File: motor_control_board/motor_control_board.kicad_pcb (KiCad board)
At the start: 4 copper layers, 45 x 40 mm, 78 parts, among them J1 Conn_01x05_Female, J2 Conn_01x05_Female, J3 Harwin_G125-MG10605M4P, J4 Harwin_M80-5000000M5-02-333-0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, J5 Harwin_M80-5400642, J6 Harwin_M80-8510442, J7 Harwin_M80-8510442, U1 CPC1117N, U2 MCP2562, U3 PIC18F26K83, U4 MCP2562, U5 PIC18F26K83, U6 SN74LVC1G14DBV, U7 INA232AIDDFR, U8 UA78M05IDCYR, U9 ECH8420-TL-H, X1 12MHz, X2 12MHz

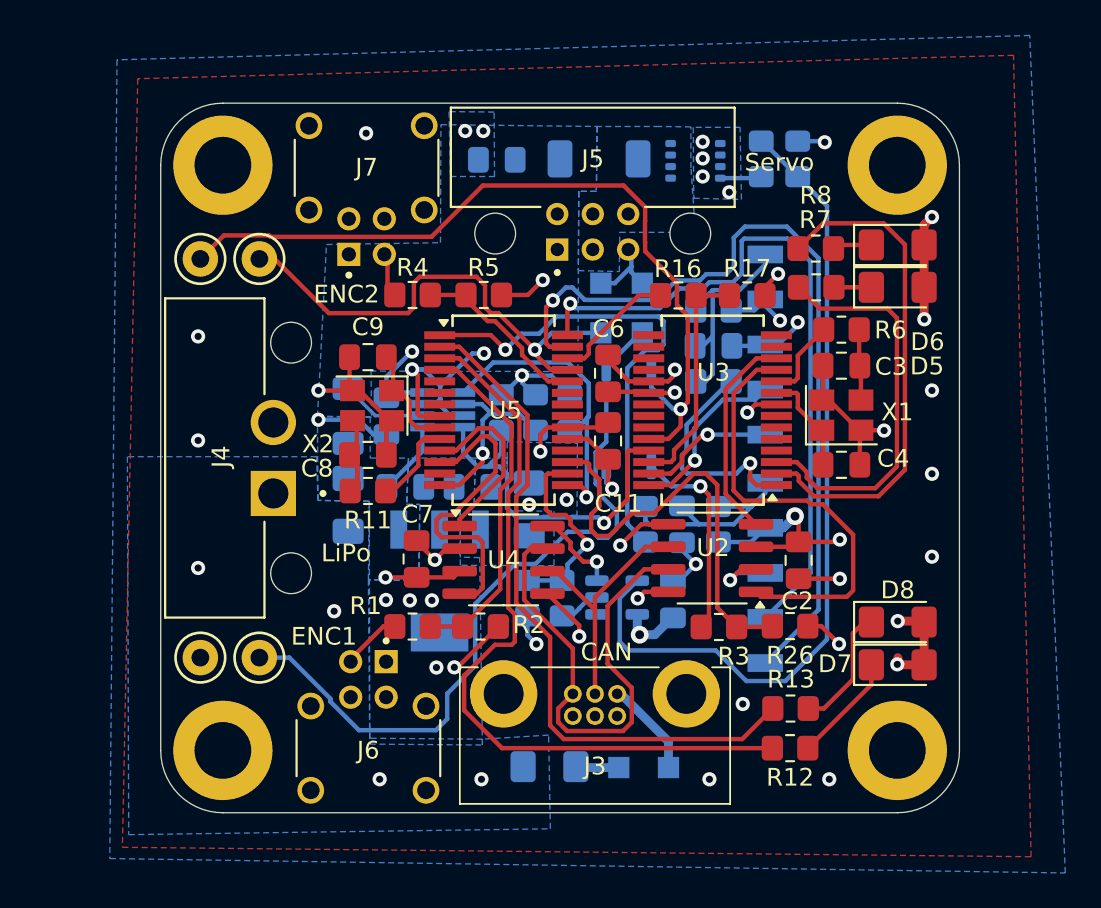
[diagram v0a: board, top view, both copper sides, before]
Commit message: Added servo power LED, bulk decoupling caps
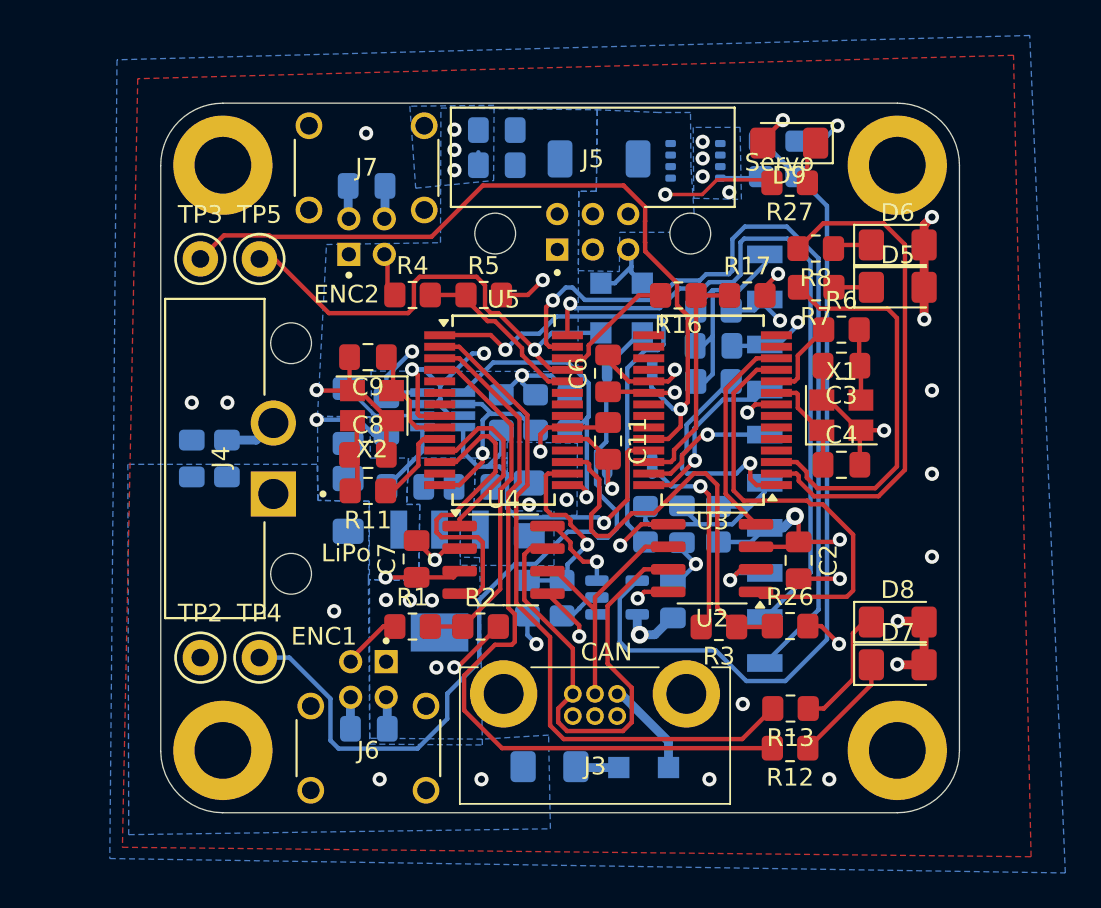
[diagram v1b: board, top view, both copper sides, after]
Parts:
- added C16: 100n, Capacitor_SMD:C_0805_2012Metric_Pad1.18x1.45mm_HandSolder, B.Cu at (162.2, 92.3)
- added C17: 100n, Capacitor_SMD:C_0805_2012Metric_Pad1.18x1.45mm_HandSolder, B.Cu at (162.1, 61.7)
- added C18: 22u, Capacitor_SMD:C_0805_2012Metric_Pad1.18x1.45mm_HandSolder, B.Cu at (152.2, 77.0)
- added C19: 22u, Capacitor_SMD:C_0805_2012Metric_Pad1.18x1.45mm_HandSolder, B.Cu at (154.2, 77.0)
- added C21: 22u, Capacitor_SMD:C_0805_2012Metric_Pad1.18x1.45mm_HandSolder, B.Cu at (169.4, 58.5)
- added D9: RED, LED_SMD:LED_1206_3216Metric_Pad1.42x1.75mm_HandSolder, F.Cu at (185.9, 59.3)
- added R27: 330R, Resistor_SMD:R_0805_2012Metric_Pad1.20x1.40mm_HandSolder, F.Cu at (185.9, 61.5)
- C1: value 10u -> 22u; footprint canhw_footprints:C_0805_2012Metric_Pad1.18x1.45mm_HandSolder -> Capacitor_SMD:C_0805_2012Metric_Pad1.18x1.45mm_HandSolder
- C10, C11, C12, C13, C14, C15, C2, C3, C4, C5, C6, C7, C8, C9: footprint canhw_footprints:C_0805_2012Metric_Pad1.18x1.45mm_HandSolder -> Capacitor_SMD:C_0805_2012Metric_Pad1.18x1.45mm_HandSolder
- D1, D2, D3: footprint canhw_footprints:Nexperia_CFP3_SOD-123W -> Diode_SMD:Nexperia_CFP3_SOD-123W
- D4: footprint canhw_footprints:D_SOD-128 -> Diode_SMD:D_SOD-128
- D5, D6, D7, D8: footprint canhw_footprints:LED_1206_3216Metric_Pad1.42x1.75mm_HandSolder -> LED_SMD:LED_1206_3216Metric_Pad1.42x1.75mm_HandSolder
- F1, F2, F3: footprint canhw_footprints:Fuse_1206_3216Metric_Pad1.42x1.75mm_HandSolder -> Fuse:Fuse_1206_3216Metric_Pad1.42x1.75mm_HandSolder
- H1, H2, H3, H4: footprint canhw_footprints:MountingHole_3.2mm_M3_DIN965_Pad -> MountingHole:MountingHole_3.2mm_M3_DIN965_Pad
- R1, R10, R11, R12, R13, R14, R15, R16, R17, R18, R19, R2, R20, R21, R23, R24, R25, R26, R3, R4, R5, R6, R7, R8, R9: footprint canhw_footprints:R_0805_2012Metric_Pad1.20x1.40mm_HandSolder -> Resistor_SMD:R_0805_2012Metric_Pad1.20x1.40mm_HandSolder
- R22: footprint canhw_footprints:R_1206_3216Metric_Pad1.30x1.75mm_HandSolder -> Resistor_SMD:R_1206_3216Metric_Pad1.30x1.75mm_HandSolder
- TP2, TP3, TP4, TP5: footprint canhw_footprints:TestPoint_Keystone_5000-5004_Miniature -> TestPoint:TestPoint_Keystone_5000-5004_Miniature
- U1: footprint canhw_footprints:SOP-4_3.8x4.1mm_P2.54mm -> canhw_footprints:SOIC254P610X218-4N
- U2, U4: footprint canhw_footprints:SOIC-8_3.9x4.9mm_P1.27mm -> Package_SO:SOIC-8_3.9x4.9mm_P1.27mm
- U3, U5: footprint canhw_footprints:SSOP-28_5.3x10.2mm_P0.65mm -> Package_SO:SSOP-28_5.3x10.2mm_P0.65mm
- U6: footprint canhw_footprints:SOT-23-5 -> Package_TO_SOT_SMD:SOT-23-5
- U9: footprint canhw_footprints:OnSemi_ECH8 -> Package_TO_SOT_SMD:OnSemi_ECH8
- X1, X2: footprint canhw_footprints:Crystal_SMD_Abracon_ABM8G-4Pin_3.2x2.5mm -> Crystal:Crystal_SMD_Abracon_ABM8G-4Pin_3.2x2.5mm
- moved C1 0.30 mm to (169.4, 60.5)
- moved U1 0.05 mm to (176.9, 74.7)
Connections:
- J6 pad 1: +5V -> unconnected-(J6-Pin_1-Pad1)
- J6 pad 3: GND -> +5V
- J6 pad 4: unconnected-(J6-Pin_4-Pad4) -> GND
- J7 pad 1: +5V -> unconnected-(J7-Pin_1-Pad1)
- J7 pad 3: GND -> +5V
- J7 pad 4: unconnected-(J7-Pin_4-Pad4) -> GND
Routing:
- net GND: track 84.4 -> 92.3 mm
- net /Servo-: track 0.00 -> 6.42 mm, vias 0 -> 1
- net +5V: track 62.3 -> 67.7 mm, vias 17 -> 18
- net Net-(D9-K): track 0.00 -> 2.43 mm
- net /PWM_SERVO: track 42.4 -> 44.5 mm

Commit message: silkscreen
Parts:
- added G***: LOGO, Team_Logo:Logo_SilkScreen_5mm, B.Cu at (170.6, 68.1)
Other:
- board text added: "5V"

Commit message: Free some Real estate so Joe can move in
Moved things around, generate production files
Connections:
- net /MCLR_FS renamed /Failsafe MCU/MCLR_FS
- J1 pad 1: /ICSPCLK_FS -> /Failsafe MCU/ICSPDAT_FS
- J1 pad 2: /ICSPDAT_FS -> /Failsafe MCU/ICSPCLK_FS
- U5 pad 27: /ICSPCLK_FS -> /Failsafe MCU/ICSPCLK_FS
- U5 pad 28: /ICSPDAT_FS -> /Failsafe MCU/ICSPDAT_FS
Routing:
- net (no net): track 0.00 -> 87.1 mm, vias 0 -> 2
- net /ICSPCLK_FS: track 47.2 -> 0.00 mm, vias 1 -> 0
- net /ICSPDAT_FS: track 39.9 -> 0.00 mm, vias 1 -> 0

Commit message: skill issued two pinouts
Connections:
- J1 pad 1: /Failsafe MCU/ICSPDAT_FS -> /Failsafe MCU/ICSPCLK_FS
- J1 pad 2: /Failsafe MCU/ICSPCLK_FS -> /Failsafe MCU/ICSPDAT_FS
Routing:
- net (no net): track 87.1 -> 0.00 mm, vias 2 -> 0
- net /Failsafe MCU/ICSPCLK_FS: track 0.00 -> 47.2 mm, vias 0 -> 1
- net /Failsafe MCU/ICSPDAT_FS: track 0.00 -> 39.9 mm, vias 0 -> 1

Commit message: Address concerns
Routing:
- net GND: track 92.7 -> 92.3 mm, vias 44 -> 46
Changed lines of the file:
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@@
 	)
 	(segment
+		(start 170.115863 67.818)
+		(end 171.388278 69.090415)
+		(width 0.25)
+		(layer "F.Cu")
+		(net 2)
+	)
+	(segment
 		(start 187.7861 73.6809)
 		(end 187.7236 73.7434)
@@
 	)
 	(segment
-		(start 169.656 67.818)
-		(end 171.1452 67.818)
-		(width 0.25)
-		(layer "F.Cu")
-		(net 2)
-	)
-	(segment
 		(start 179.0588 84.5566)
 		(end 177.706104 84.5566)
@@
 	)
 	(segment
-		(start 171.1452 67.818)
-		(end 171.9834 66.9798)
-		(width 0.25)
-		(layer "F.Cu")
-		(net 2)
-	)
-	(segment
 		(start 164.8714 81.6649)
 		(end 164.8714 81.723227)
@@
 	)
 	(segment
+		(start 169.656 67.818)
+		(end 170.115863 67.818)
+		(width 0.25)
+		(layer "F.Cu")
+		(net 2)
+	)
+	(segment
 		(start 177.9592 72.689)
 		(end 179.0592 72.689)
@@
 	)
 	(via
-		(at 171.9834 66.9798)
+		(at 171.388278 69.090415)
 		(size 0.8)
 		(drill 0.4)
@@
 	)
 	(via
+		(at 182.5 58)
+		(size 0.8)
+		(drill 0.4)
+		(layers "F.Cu" "B.Cu")
+		(free yes)
+		(net 2)
+	)
+	(via
 		(at 165.989 88.8238)
 		(size 0.8)
@@
 	)
 	(via
+		(at 181.5 58)
+		(size 0.8)
+		(drill 0.4)
+		(layers "F.Cu" "B.Cu")
+		(free yes)
+		(net 2)
+	)
+	(via
 		(at 167.132 60.7822)
 		(size 0.8)
@@
 		(polygon
 			(pts
-				(xy 162.3314 74.7014) (xy 159.2834 74.676) (xy 159.7914 64.9732) (xy 166.2176 64.8716) (xy 166.243 57.277)
-				(xy 175.0568 57.3786) (xy 175.006 61.976) (xy 174.0154 61.976) (xy 173.9646 72.136) (xy 162.306 72.1106)
+				(xy 162.3314 74.7014) (xy 159.2834 74.676) (xy 160 63) (xy 166 62) (xy 166.243 57.277) (xy 175.0568 57.3786)
+				(xy 175.006 61.976) (xy 174.0154 61.976) (xy 173.9646 72.136) (xy 162.306 72.1106)
 			)
 		)

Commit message: addressed concerns
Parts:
- added C20: 22u, canhw_footprints:C_0805_2012Metric_Pad1.18x1.45mm_HandSolder, B.Cu at (148.1, 77.0)
- C1, C10, C11, C12, C13, C14, C15, C16, C17, C18, C19, C2, C21, C3, C4, C5, C6, C7, C8, C9: footprint Capacitor_SMD:C_0805_2012Metric_Pad1.18x1.45mm_HandSolder -> canhw_footprints:C_0805_2012Metric_Pad1.18x1.45mm_HandSolder
- D1, D2, D3: footprint Diode_SMD:Nexperia_CFP3_SOD-123W -> canhw_footprints:Nexperia_CFP3_SOD-123W
- D4: footprint Diode_SMD:D_SOD-128 -> canhw_footprints:D_SOD-128
- D5, D6, D7, D8, D9: footprint LED_SMD:LED_1206_3216Metric_Pad1.42x1.75mm_HandSolder -> canhw_footprints:LED_1206_3216Metric_Pad1.42x1.75mm_HandSolder
- F1, F2: footprint Fuse:Fuse_1206_3216Metric_Pad1.42x1.75mm_HandSolder -> canhw_footprints:Fuse_1206_3216Metric_Pad1.42x1.75mm_HandSolder
- F3: value Polyfuse 1A -> Polyfuse 0.5A; footprint Fuse:Fuse_1206_3216Metric_Pad1.42x1.75mm_HandSolder -> canhw_footprints:Fuse_1206_3216Metric_Pad1.42x1.75mm_HandSolder
- H1, H2, H3, H4: footprint MountingHole:MountingHole_3.2mm_M3_DIN965_Pad -> canhw_footprints:MountingHole_3.2mm_M3_DIN965_Pad
- J4: footprint canhw_footprints:HARWIN_M80-5000000M5-02-333-00-000 -> canhw_footprints:TE_2-1437667-4
- R1, R10, R11, R12, R13, R14, R15, R16, R17, R18, R19, R2, R20, R21, R23, R24, R25, R26, R27, R3, R4, R5, R6, R7, R8, R9: footprint Resistor_SMD:R_0805_2012Metric_Pad1.20x1.40mm_HandSolder -> canhw_footprints:R_0805_2012Metric_Pad1.20x1.40mm_HandSolder
- R22: footprint Resistor_SMD:R_1206_3216Metric_Pad1.30x1.75mm_HandSolder -> canhw_footprints:R_1206_3216Metric_Pad1.30x1.75mm_HandSolder
- TP2, TP3, TP4, TP5: footprint TestPoint:TestPoint_Keystone_5000-5004_Miniature -> canhw_footprints:TestPoint_Keystone_5000-5004_Miniature
- U2, U4: footprint Package_SO:SOIC-8_3.9x4.9mm_P1.27mm -> canhw_footprints:SOIC-8_3.9x4.9mm_P1.27mm
- U3, U5: footprint Package_SO:SSOP-28_5.3x10.2mm_P0.65mm -> canhw_footprints:SSOP-28_5.3x10.2mm_P0.65mm
- U6: footprint Package_TO_SOT_SMD:SOT-23-5 -> canhw_footprints:SOT-23-5
- U9: footprint Package_TO_SOT_SMD:OnSemi_ECH8 -> canhw_footprints:OnSemi_ECH8
- X1, X2: footprint Crystal:Crystal_SMD_Abracon_ABM8G-4Pin_3.2x2.5mm -> canhw_footprints:Crystal_SMD_Abracon_ABM8G-4Pin_3.2x2.5mm
- moved TP3 5.39 mm to (147.3, 65.9)
- moved TP5 5.39 mm to (150.6, 65.9)
- moved TP2 5.39 mm to (147.3, 88.3)
- moved TP4 5.39 mm to (150.6, 88.3)
- moved H2 5.11 mm to (148.8, 60.5)
- moved H3 5.11 mm to (148.8, 93.5)
- moved J4 4.11 mm to (156.0, 73.0)
- moved G*** 2.54 mm to (168.1, 68.5)
- moved C18 1.94 mm to (150.3, 77.0)
- moved C19 1.78 mm to (152.4, 77.0)
- moved D9 0.18 mm to (185.7, 59.3)
- moved J6 0.13 mm to (162.0, 93.3)
- moved R1 0.13 mm to (164.8, 86.5)
- moved H1 0.05 mm to (192.0, 60.5)
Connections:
- net /ENC1_IN renamed Net-(J6-Pin_2)
- net /ENC2_IN renamed Net-(J7-Pin_2)
- net /Power/LDO_OUT renamed Net-(U8-OUTPUT)
- J4 pad 1: /Batt+ -> GND
- J4 pad 2: GND -> /Batt+
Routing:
- net /PWM_FS: track 27.4 -> 32.8 mm
- net /PWM_MCU: track 46.3 -> 51.7 mm
- net /PWM_SERVO: track 44.5 -> 49.8 mm
- net GND: track 92.3 -> 89.0 mm
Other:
- board size 45 x 40 mm -> 50.2 x 40 mm
- board text added: "+"
- board text added: "MCLR"
- board text added: "Motor Control"
- board text removed: "Missile Control"

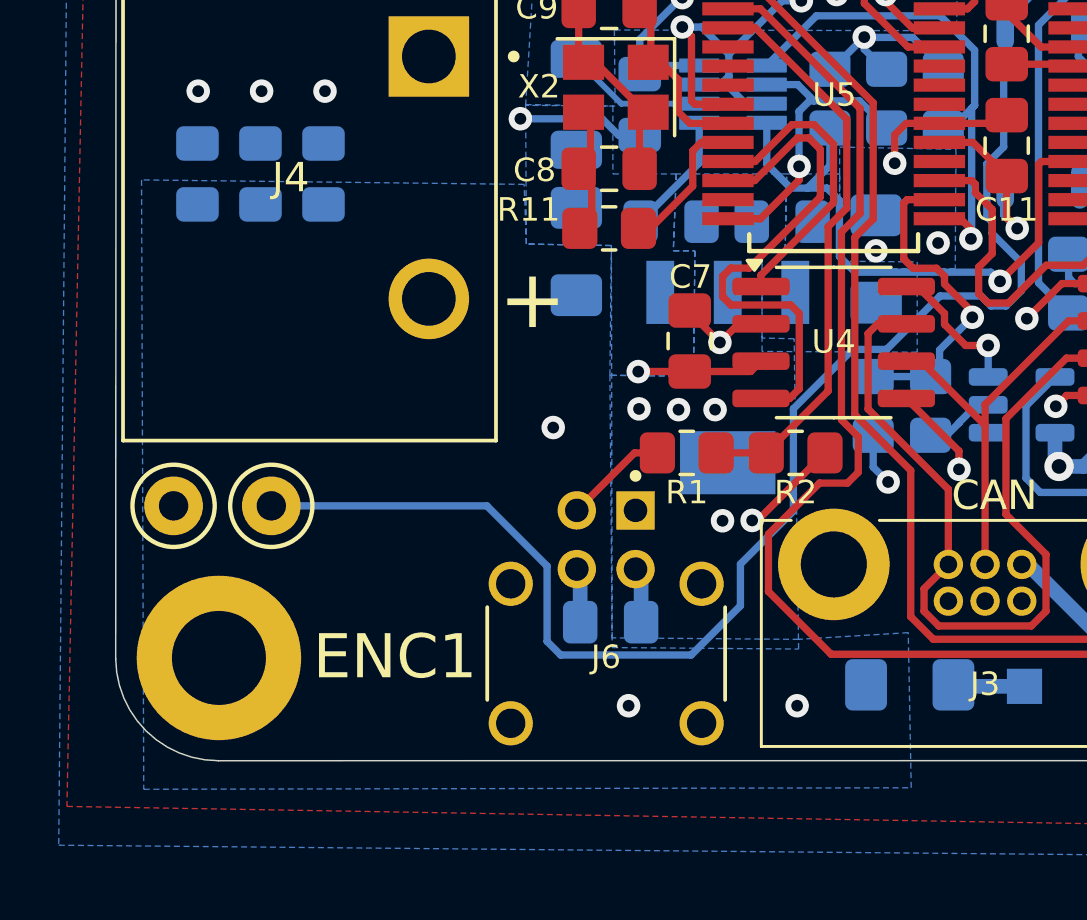
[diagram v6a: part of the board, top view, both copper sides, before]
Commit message: minor schematic and copper pour cleanup
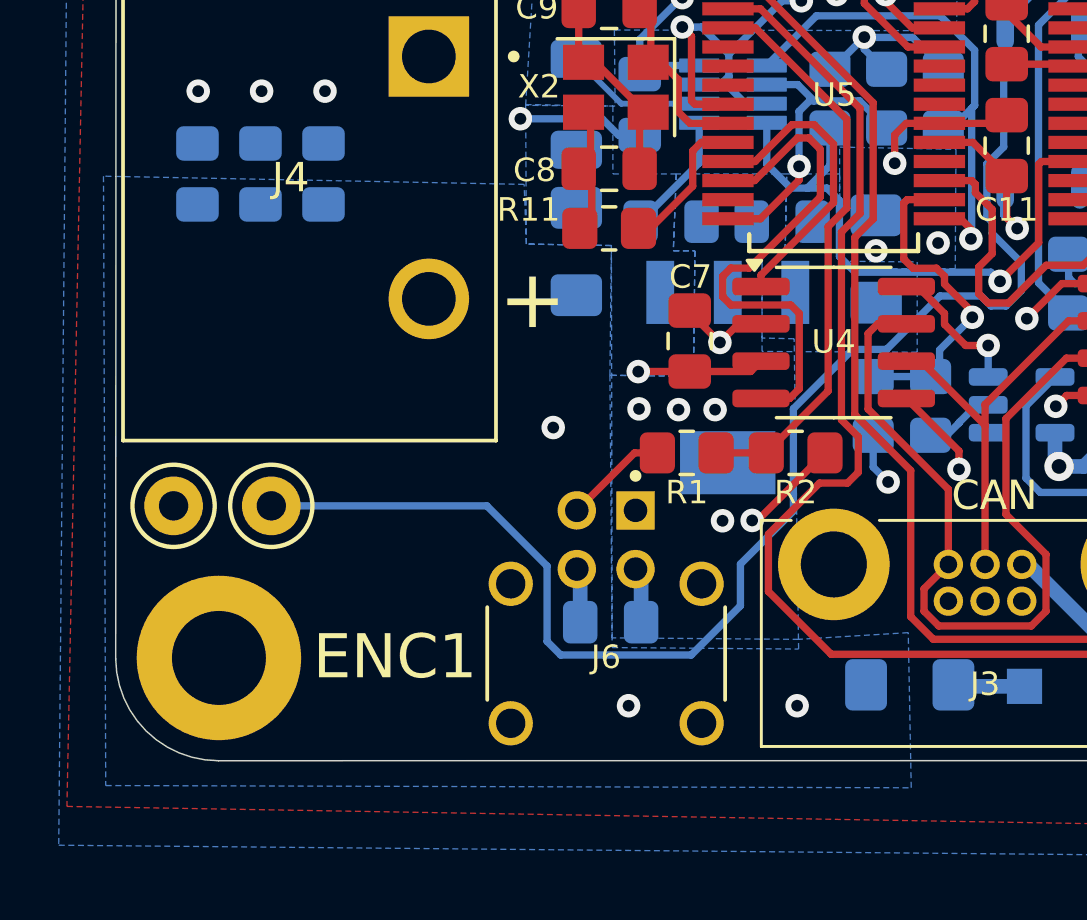
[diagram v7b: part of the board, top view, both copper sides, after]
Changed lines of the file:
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@@
 		(polygon
 			(pts
-				(xy 159.2326 77.3684) (xy 146.2024 77.216) (xy 146.2786 97.9678) (xy 172.4152 97.917) (xy 172.3136 92.6338)
+				(xy 159.2326 77.3684) (xy 144.907 77.089) (xy 144.9832 97.8408) (xy 172.4152 97.917) (xy 172.3136 92.6338)
 				(xy 168.5798 92.8624) (xy 162.2298 92.8116) (xy 162.2044 79.4512) (xy 159.3088 79.4004)
 			)

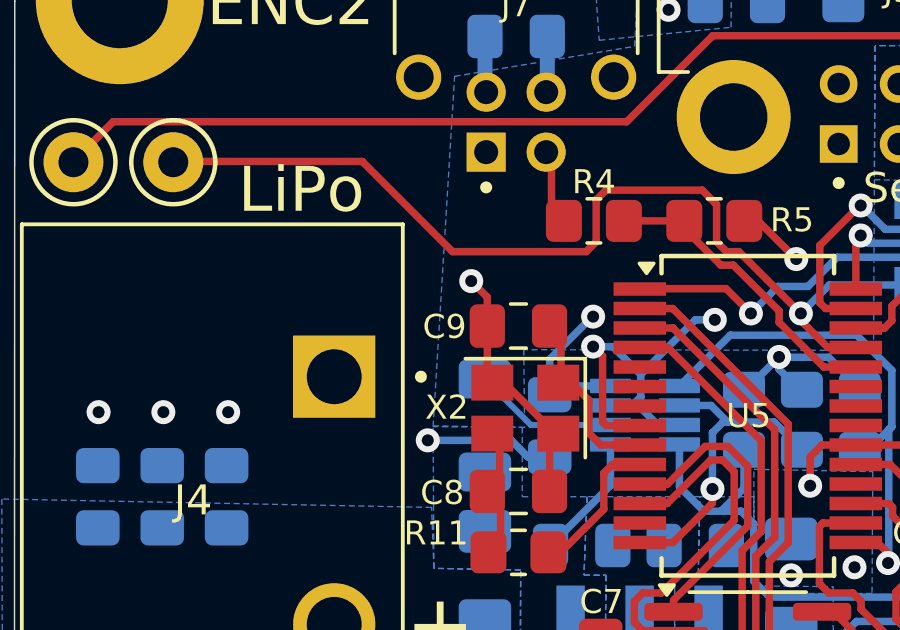
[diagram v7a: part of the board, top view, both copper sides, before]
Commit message: moved via for finn
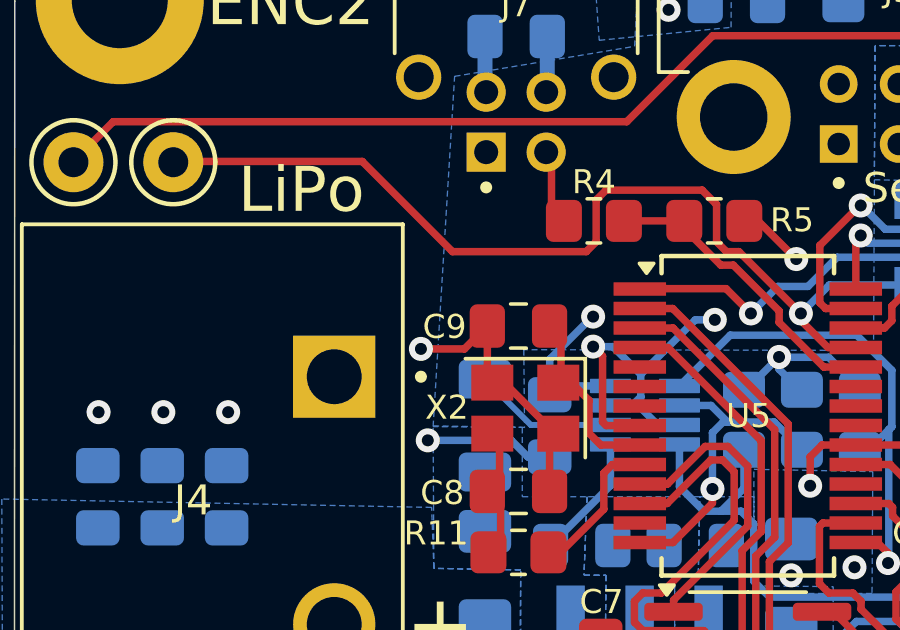
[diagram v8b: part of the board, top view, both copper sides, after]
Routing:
- net GND: track 89.0 -> 89.8 mm
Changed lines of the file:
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@@
-	)
-	(segment
-		(start 161.0907 71.3232)
-		(end 161.0907 70.3619)
-		(width 0.25)
-		(layer "F.Cu")
-		(net 2)
 	)
 	(segment
@@
 	)
 	(segment
-		(start 161.0907 70.3619)
-		(end 160.5534 69.8246)
-		(width 0.25)
-		(layer "F.Cu")
-		(net 2)
-	)
-	(segment
 		(start 174.5203 75.939)
 		(end 175.6664 77.0851)
@@
 	)
 	(segment
+		(start 158.877 72.0852)
+		(end 160.3287 72.0852)
+		(width 0.25)
+		(layer "F.Cu")
+		(net 2)
+	)
+	(segment
 		(start 163.3568 74.91)
 		(end 161.6568 73.21)
@@
 	)
 	(segment
+		(start 160.3287 72.0852)
+		(end 161.0907 71.3232)
+		(width 0.25)
+		(layer "F.Cu")
+		(net 2)
+	)
+	(segment
 		(start 188.7319 83.8161)
 		(end 188.7358 83.82)
@@
 	)
 	(via
-		(at 160.5534 69.8246)
-		(size 0.8)
-		(drill 0.4)
+		(at 158.877 72.0852)
+		(size 0.8)
+		(drill 0.4)
